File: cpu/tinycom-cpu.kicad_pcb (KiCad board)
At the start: 4 copper layers, 39.9 x 41.4 mm, 23 parts, among them P1 CONN_02X08, P2 CONN_02X08, U1 OLIMEX_IC_A13, U2 H5TQ2G83BFR/FBGA82, Y1 Crystal

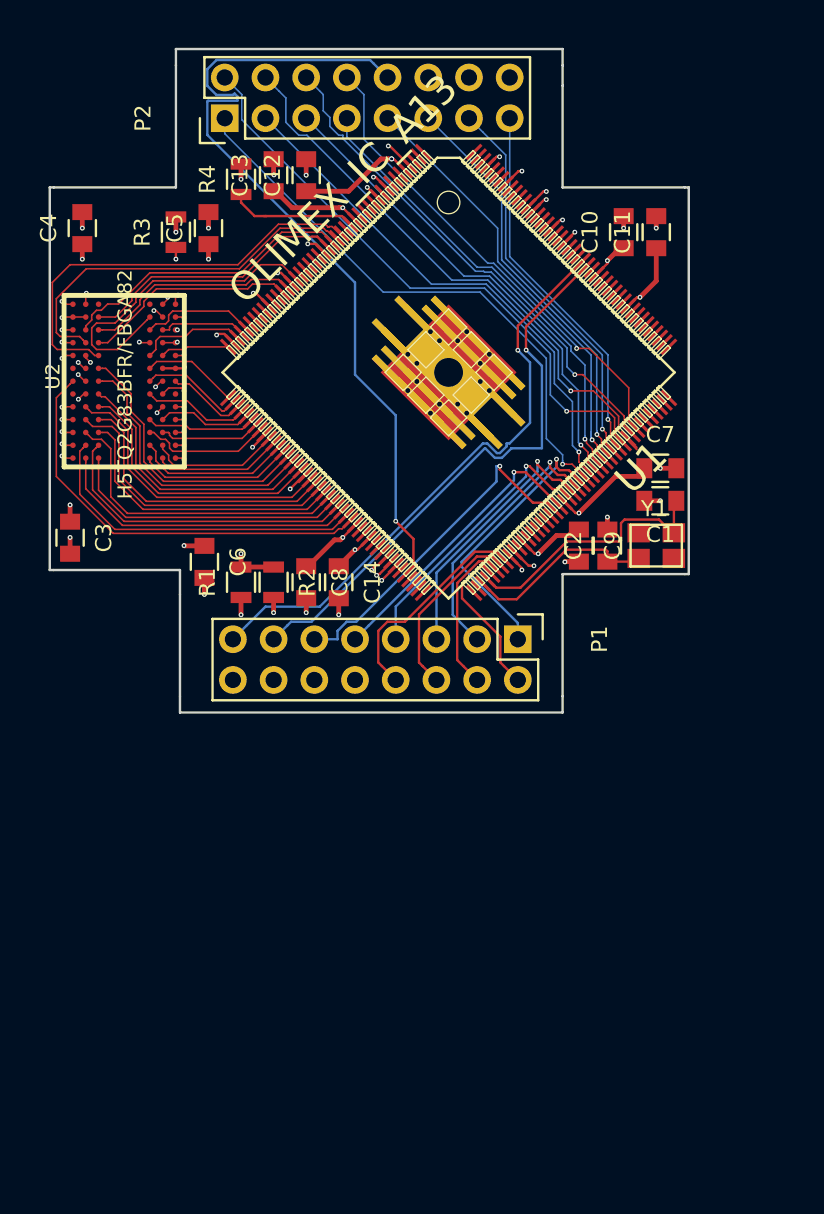
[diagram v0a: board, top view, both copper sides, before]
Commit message: ddr 4mil->6mil tracks, closer to cpu
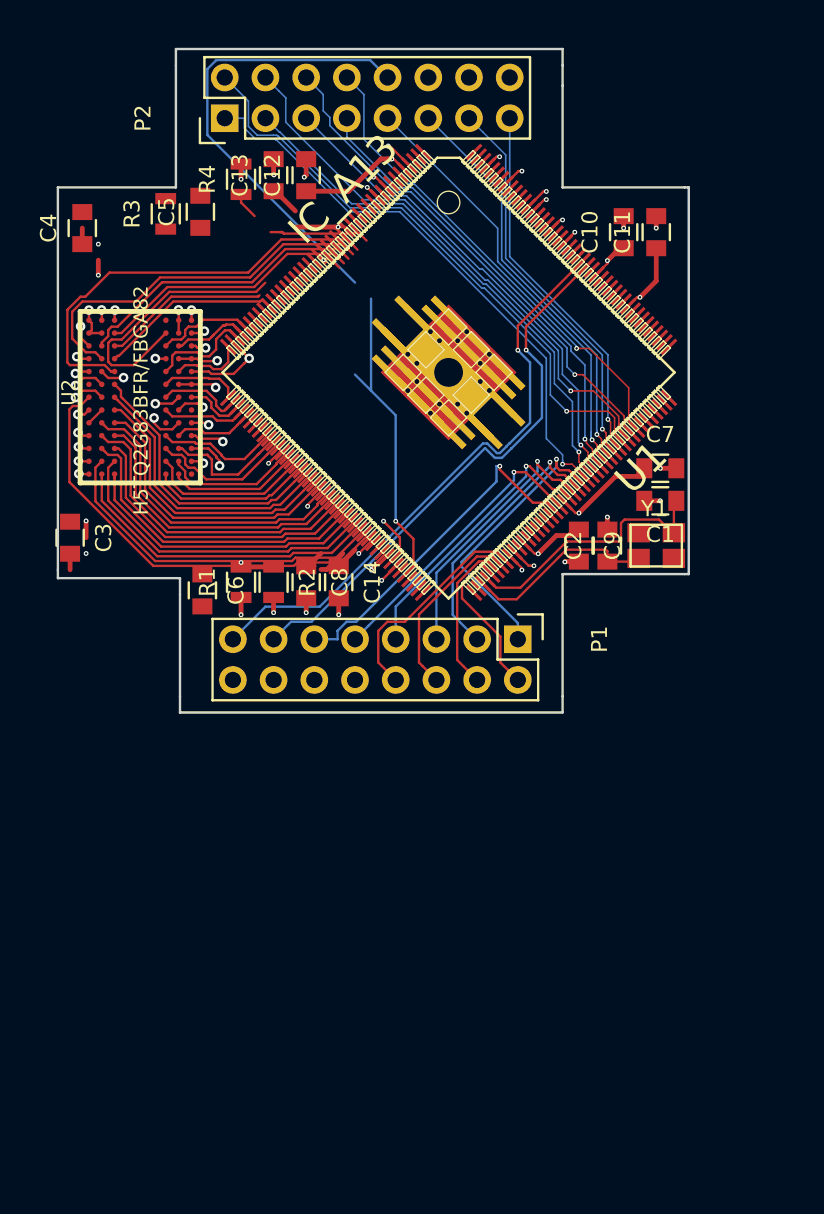
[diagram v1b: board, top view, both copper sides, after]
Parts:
- U1: value OLIMEX_IC_A13 -> IC_A13
- moved C6 1.78 mm to (88.0, 124.2)
- moved U2 1.41 mm to (80.9, 107.3)
- moved R3 1.31 mm to (85.7, 100.7)
- moved C5 1.14 mm to (87.9, 100.6)
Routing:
- net VCC_30: track 1.33 -> 53.3 mm
- net VCC_15: track 70.0 -> 34.1 mm, vias 23 -> 19
- net Net-(R1-Pad2): track 25.6 -> 5.98 mm
- net (no net): track 0.03 -> 8.18 mm
- net Net-(R3-Pad1): track 11.2 -> 4.91 mm, vias 2 -> 1
- net GND: track 28.6 -> 32.7 mm, vias 34 -> 26
- net DDR3_DM0: track 20.6 -> 17.0 mm
- net MICIN1: track 52.4 -> 49.0 mm
- net DDR3_DQS0_P: track 13.5 -> 10.4 mm
- net DDR3_DQS0_N: track 13.4 -> 10.7 mm
- net VCC_33: track 97.4 -> 94.9 mm
- net CSI_D5: track 36.1 -> 34.3 mm
- net DDR3_A4: track 6.35 -> 8.00 mm
- net DDR3_A10: track 6.63 -> 5.24 mm
- net DDR3_CKE: track 4.96 -> 3.75 mm
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- added copper zone on In1.Cu, net GND
- added copper zone on In2.Cu, net VCC_33
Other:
- board size 39.9 x 41.4 mm -> 39.4 x 41.4 mm
- net class Default: via_dia 0.3 -> 0.6; via_drill 0.15 -> 0.3
- net class power removed

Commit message: xxx
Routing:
- net (no net): track 8.18 -> 61.1 mm, vias 0 -> 8
- net DDR3_ODT: track 27.5 -> 0.78 mm
- net VCC_30: track 53.3 -> 27.3 mm
- net VCC_14: track 126.3 -> 140.4 mm, vias 12 -> 10
- net DDR3_D4: track 26.7 -> 36.1 mm, vias 0 -> 1
- net VCC_15: track 34.1 -> 26.9 mm, vias 19 -> 14
- net Net-(R4-Pad1): track 8.09 -> 1.70 mm
- net MICIN1: track 49.0 -> 43.3 mm
- net DDR3_DQS0_N: track 10.7 -> 5.14 mm
- net DDR3_D11: track 0.00 -> 3.84 mm, vias 0 -> 1
- net Net-(R3-Pad1): track 4.91 -> 1.82 mm
- net GND: track 32.7 -> 34.0 mm, vias 26 -> 25
- net DDR3_A4: track 8.00 -> 6.99 mm
- net VCC_33: track 94.9 -> 95.9 mm, vias 9 -> 8
- net DDR3_A1: track 8.76 -> 8.26 mm
- removed copper zone on In1.Cu, net GND
- removed copper zone on In2.Cu, net VCC_15
- removed copper zone on In2.Cu, net VCC_33

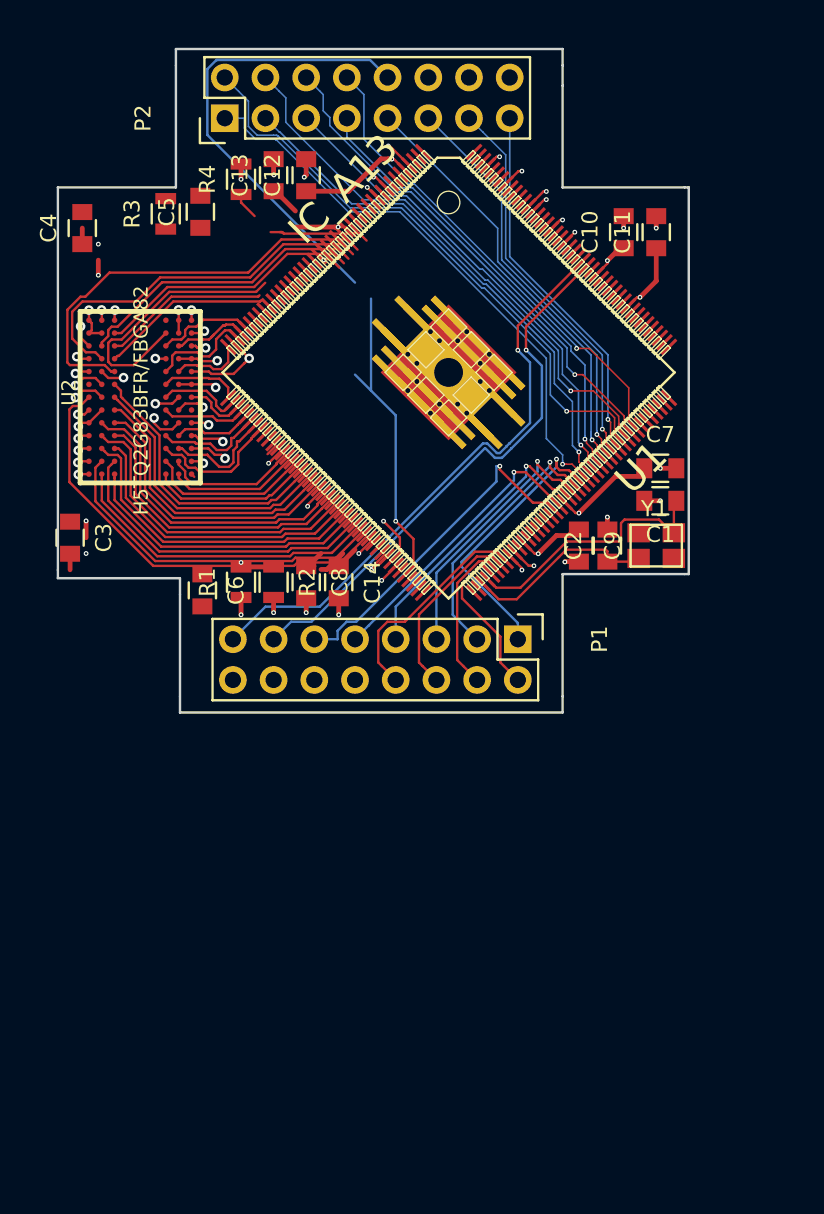
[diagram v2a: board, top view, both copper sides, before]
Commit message: change other routes to 6mil
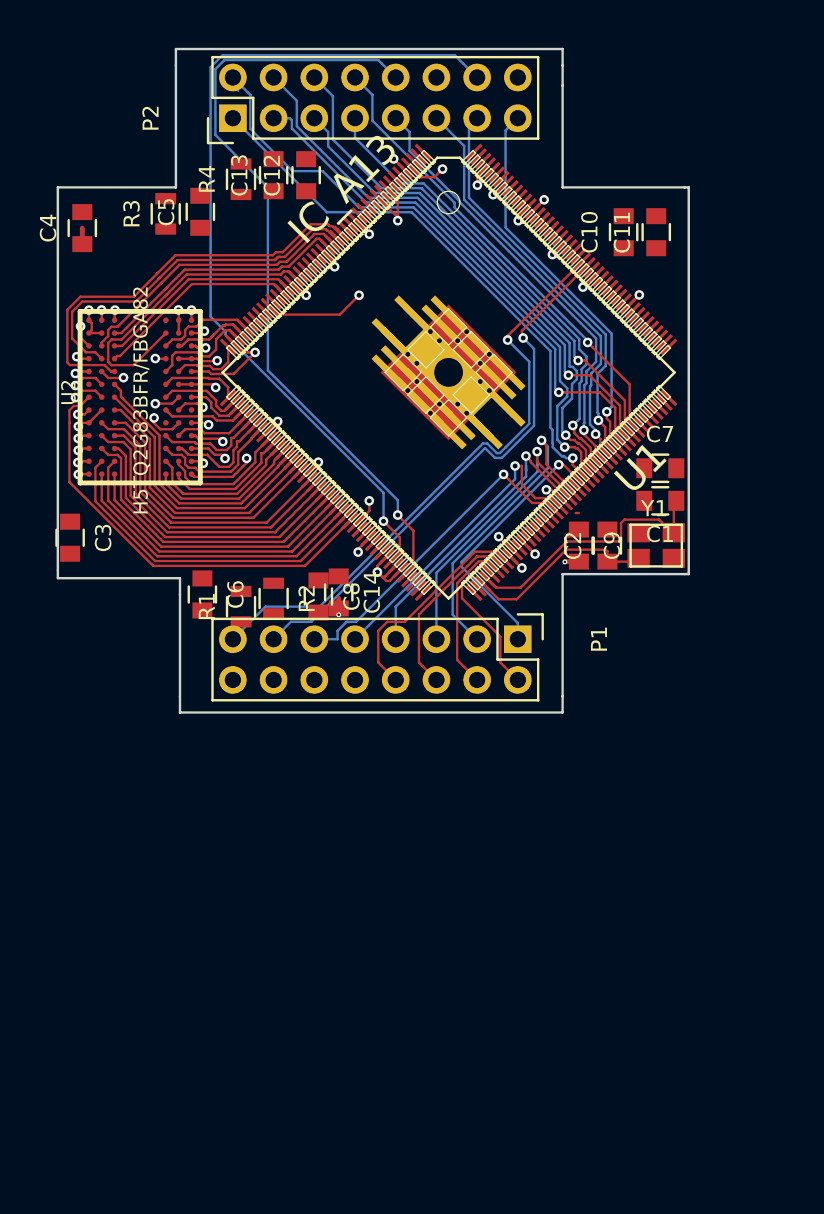
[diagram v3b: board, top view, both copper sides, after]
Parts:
- moved R1 1.52 mm to (90.4, 125.2)
- moved C8 1.17 mm to (95.2, 124.6)
- moved R2 1.02 mm to (92.5, 124.7)
- moved C14 0.64 mm to (96.5, 124.3)
- moved P2 0.51 mm to (89.9, 94.7)
- moved C6 0.25 mm to (88.0, 124.5)
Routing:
- net VCC_14: track 140.4 -> 25.5 mm, vias 10 -> 12
- net VCC_33: track 95.9 -> 11.8 mm, vias 8 -> 7
- net (no net): track 61.1 -> 8.18 mm, vias 8 -> 0
- net VCC_30: track 27.3 -> 53.4 mm
- net DDR3_ODT: track 0.78 -> 26.9 mm
- net DDR3_D4: track 36.1 -> 26.2 mm, vias 1 -> 0
- net GND: track 34.0 -> 25.4 mm, vias 25 -> 15
- net DDR3_DQS0_N: track 5.14 -> 12.6 mm
- net MICIN1: track 43.3 -> 48.8 mm
- net DDR3_D11: track 3.84 -> 0.00 mm, vias 1 -> 0
- net SDC0_D3: track 16.8 -> 19.9 mm
- net Net-(R1-Pad2): track 5.98 -> 3.12 mm, vias 3 -> 2
- net DDR3_DM0: track 17.0 -> 19.8 mm
- net DDR3_DQS0_P: track 10.4 -> 12.7 mm
- net Net-(R4-Pad1): track 1.70 -> 0.00 mm
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- added copper zone on In2.Cu, net VCC_14
- added copper zone on In2.Cu, net VCC_15
- added copper zone on In2.Cu, net VCC_33

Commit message: add power planes
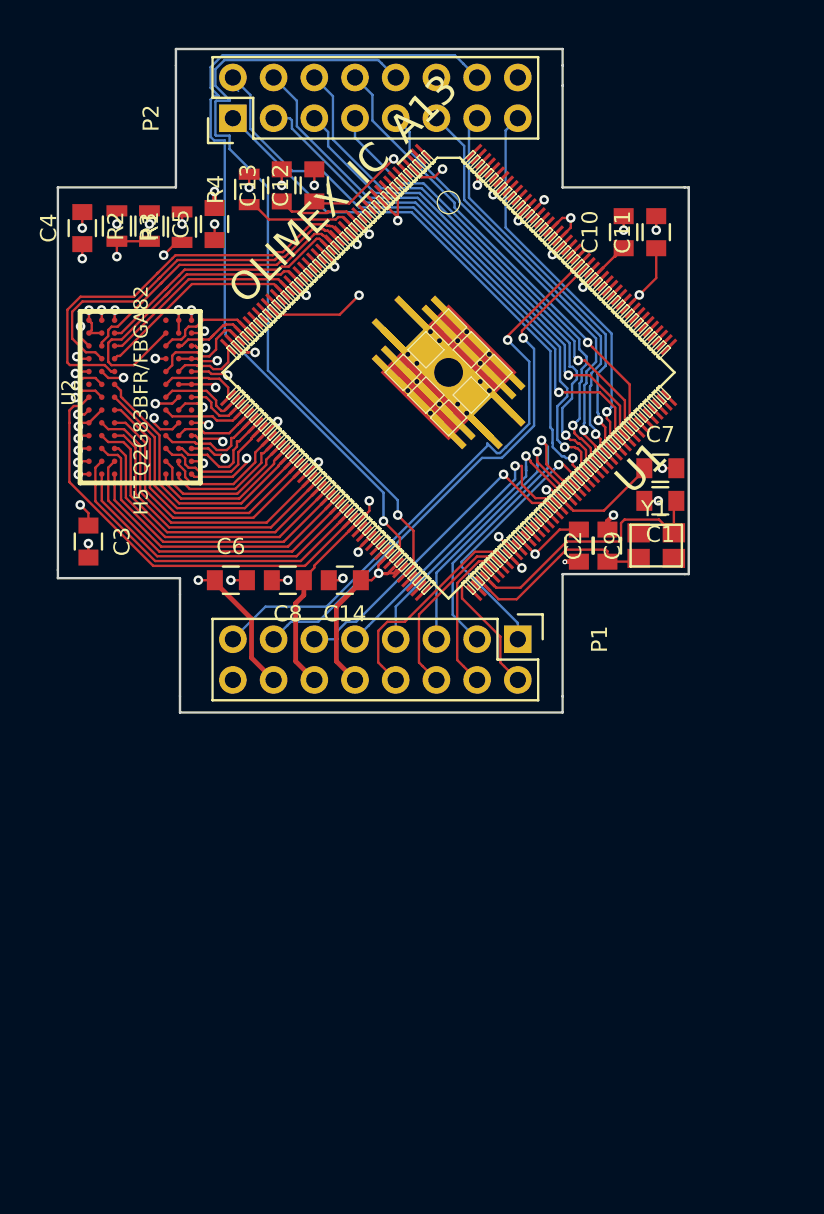
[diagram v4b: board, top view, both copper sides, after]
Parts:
- U1: value IC_A13 -> OLIMEX_IC_A13
- moved R1 25.0 mm to (82.7, 101.5), turned to 270 degrees
- moved R2 24.5 mm to (84.7, 101.5), turned to 90 degrees
- moved C8 2.16 mm to (93.3, 123.6), turned to 180 degrees
- moved C6 1.99 mm to (89.8, 123.6), turned to 0 degrees
- moved R3 1.31 mm to (86.7, 101.5)
- moved C5 1.17 mm to (88.8, 101.3)
- moved C3 1.17 mm to (80.9, 121.2)
- moved C14 0.85 mm to (96.9, 123.6), turned to 180 degrees
- moved C12 0.81 mm to (95.0, 98.9)
- moved C13 0.81 mm to (93.0, 98.9)
- moved R4 0.81 mm to (90.9, 99.2)
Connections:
- P1 pad 10: VCC_14 -> VCC_33
- P1 pad 12: VCC_33 -> VCC_14
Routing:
- net VCC_14: track 25.5 -> 50.8 mm
- net GND: track 25.4 -> 48.5 mm, vias 15 -> 32
- net VCC_15: track 26.1 -> 46.4 mm, vias 17 -> 23
- net VCC_33: track 11.8 -> 31.6 mm
- net Net-(R1-Pad2): track 3.12 -> 20.9 mm, vias 2 -> 3
- net Net-(R3-Pad1): track 1.82 -> 13.8 mm, vias 1 -> 2
- net Net-(R4-Pad1): track 0.00 -> 6.97 mm
- net MICIN1: track 48.8 -> 50.5 mm
- net VCC_30: track 53.4 -> 54.4 mm
- added copper zone on In1.Cu, net GND
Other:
- net class Default: trace_width 0.15 -> 0.3

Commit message: adjust
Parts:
- U1: value OLIMEX_IC_A13 -> IC_A13
- moved C1 29.9 mm to (122.9, 147.8)
- moved C14 29.9 mm to (103.3, 152.8)
- moved C2 29.9 mm to (119.6, 150.6)
- moved C4 29.9 mm to (86.9, 130.8)
- moved C5 29.9 mm to (95.1, 130.6)
- moved C6 29.9 mm to (96.1, 152.8)
- moved C8 29.9 mm to (99.7, 152.8)
- moved C9 29.9 mm to (117.9, 150.6)
- moved U1 29.9 mm to (109.7, 139.8)
- moved Y1 29.9 mm to (122.7, 150.6)
- moved C10 29.9 mm to (120.7, 131.1)
- moved C11 29.9 mm to (122.7, 131.1)
- moved C12 29.9 mm to (101.3, 128.1)
- moved C7 29.9 mm to (122.9, 145.8)
- moved P1 29.9 mm to (114.0, 156.5)
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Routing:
- net MICIN1: track 50.5 -> 49.0 mm
- net VCC_30: track 54.4 -> 53.4 mm
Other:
- net class Default: trace_width 0.3 -> 0.15
